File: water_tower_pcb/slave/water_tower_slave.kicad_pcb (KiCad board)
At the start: 2 copper layers, 180 x 120 mm, 7 parts, among them J1 CONN_POWER, J2 CONN_SENSOR, K1 Relay_5V, SW1 DIP_8P, U1 AMS1117-3.3, U2 STC32G12K128, U3 PAN3031

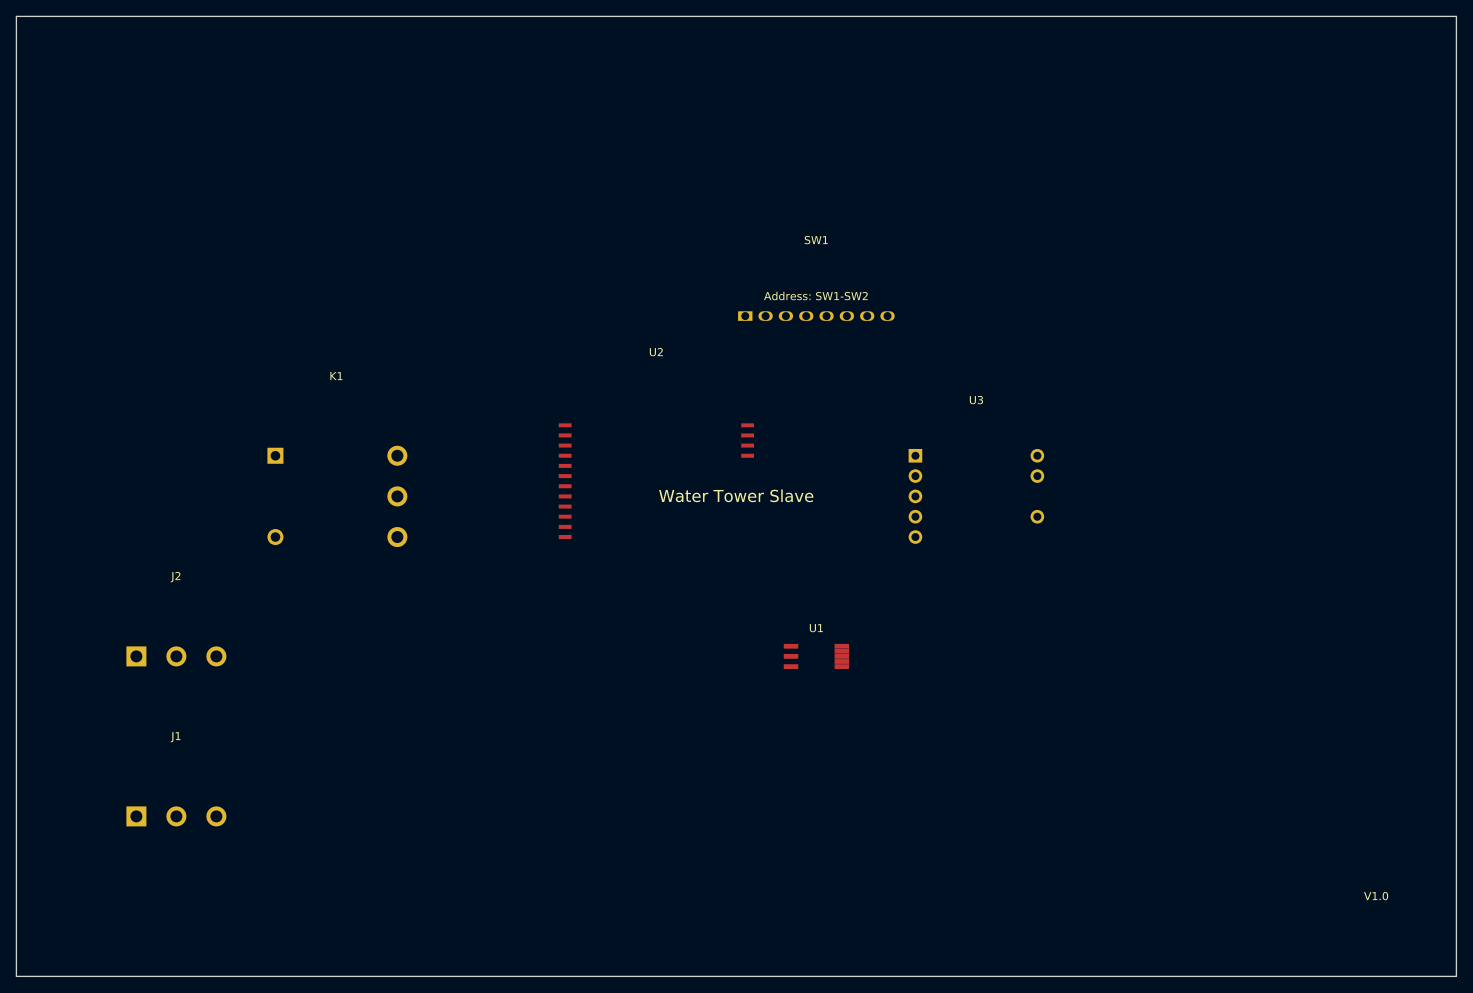
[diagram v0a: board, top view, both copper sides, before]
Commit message: feat: 系统架构变更 v2.0 - ESP8266 控制水泵
重大变更:
- 水泵控制权从 STC8G 从机转移到 ESP8266 主机
- STC8G 从机只负责传感器数据采集
- 简化从机设计，降低成本，提升可靠性

固件变更:
- esp8266_master: 已包含继电器控制 (GPIO16)
- slave_node_stc8g: 移除水泵控制，只读传感器

文档更新:
- 新增 SYSTEM_ARCHITECTURE.md (系统架构与需求)
- 新增 ELECTRICAL_SYSTEM.md (电器系统图)
- 新增 PCB_UPDATE_NEEDED.md (PCB 更新清单)
- 新增 CHANGELOG_v2.0.md (变更总结)
- 更新所有 STC32G 引用为 STC8G1K08

BOM 更新:
- 从机移除继电器相关元件
- 单台成本降低 ¥13

注意:
- 从机 PCB 需要用 KiCad 更新 (移除继电器封装)
- 临时方案：使用现有 PCB 但不焊接继电器部分
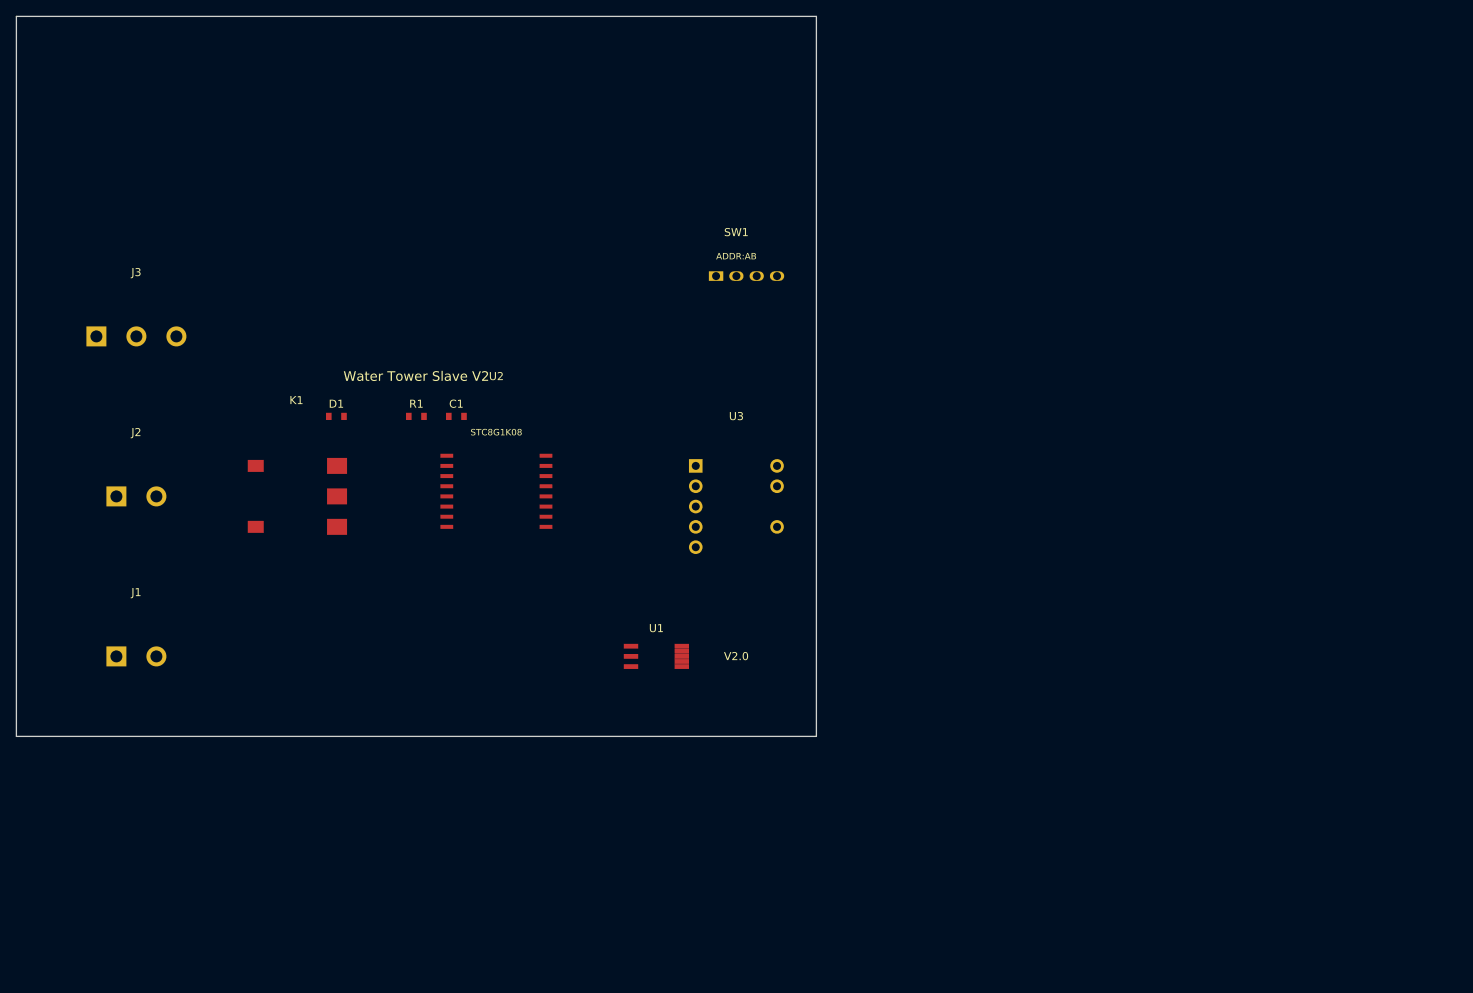
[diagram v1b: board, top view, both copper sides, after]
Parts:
- added C1: 100nF, Capacitor_SMD:C_0805_2012Metric, F.Cu at (55.0, 50.0)
- added D1: 1N4148, Diode_SMD:D_SOD-323, F.Cu at (40.0, 50.0)
- added R1: 10k, Resistor_SMD:R_0805_2012Metric, F.Cu at (50.0, 50.0)
- added SW1: DIP_2P, Switch:DIP_Switch_2P, F.Cu at (90.0, 35.0)
- J1: footprint Connector:TerminalBlock_3P_5mm -> Connector:TerminalBlock_2P_5mm
- J2: value CONN_SENSOR -> CONN_PUMP; footprint Connector:TerminalBlock_3P_5mm -> Connector:TerminalBlock_2P_5mm
- J3: renamed from SW1; value DIP_8P -> CONN_SENSOR; footprint Switch:DIP_Switch_8P -> Connector:TerminalBlock_3P_5mm
- K1: footprint Relay:Relay_SPDT_5V -> Relay:Relay_SPDT_5V_SMD
- U2: value STC32G12K128 -> STC8G1K08; footprint water_tower:STC32G_LQFP48 -> water_tower:STC8G1K08_SOP16
- moved J3 85.0 mm to (15.0, 40.0)
- moved U3 30.0 mm to (90.0, 60.0)
- moved J1 20.6 mm to (15.0, 80.0)
- moved J2 20.6 mm to (15.0, 60.0)
- moved U1 20.0 mm to (80.0, 80.0)
- moved U2 20.0 mm to (60.0, 60.0)
- moved K1 5.00 mm to (35.0, 60.0)
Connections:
- J2 pad 1: SENSOR_VCC -> PUMP_CTRL
- J2 pad 2: SENSOR_GND -> +12V
- J3 pad 1: DIP_A -> +5V
- J3 pad 2: DIP_B -> GND
- J3 pad 3: GND -> ADC_IN
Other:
- board size 180 x 120 mm -> 100 x 90 mm
- board text added: "ADDR:AB"
- board text added: "STC8G1K08"
- board text added: "V2.0"
- board text added: "Water Tower Slave V2"
- board text removed: "Address: SW1-SW2"
- board text removed: "V1.0"
- board text removed: "Water Tower Slave"
